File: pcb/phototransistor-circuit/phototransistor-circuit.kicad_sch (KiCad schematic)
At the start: 5 parts

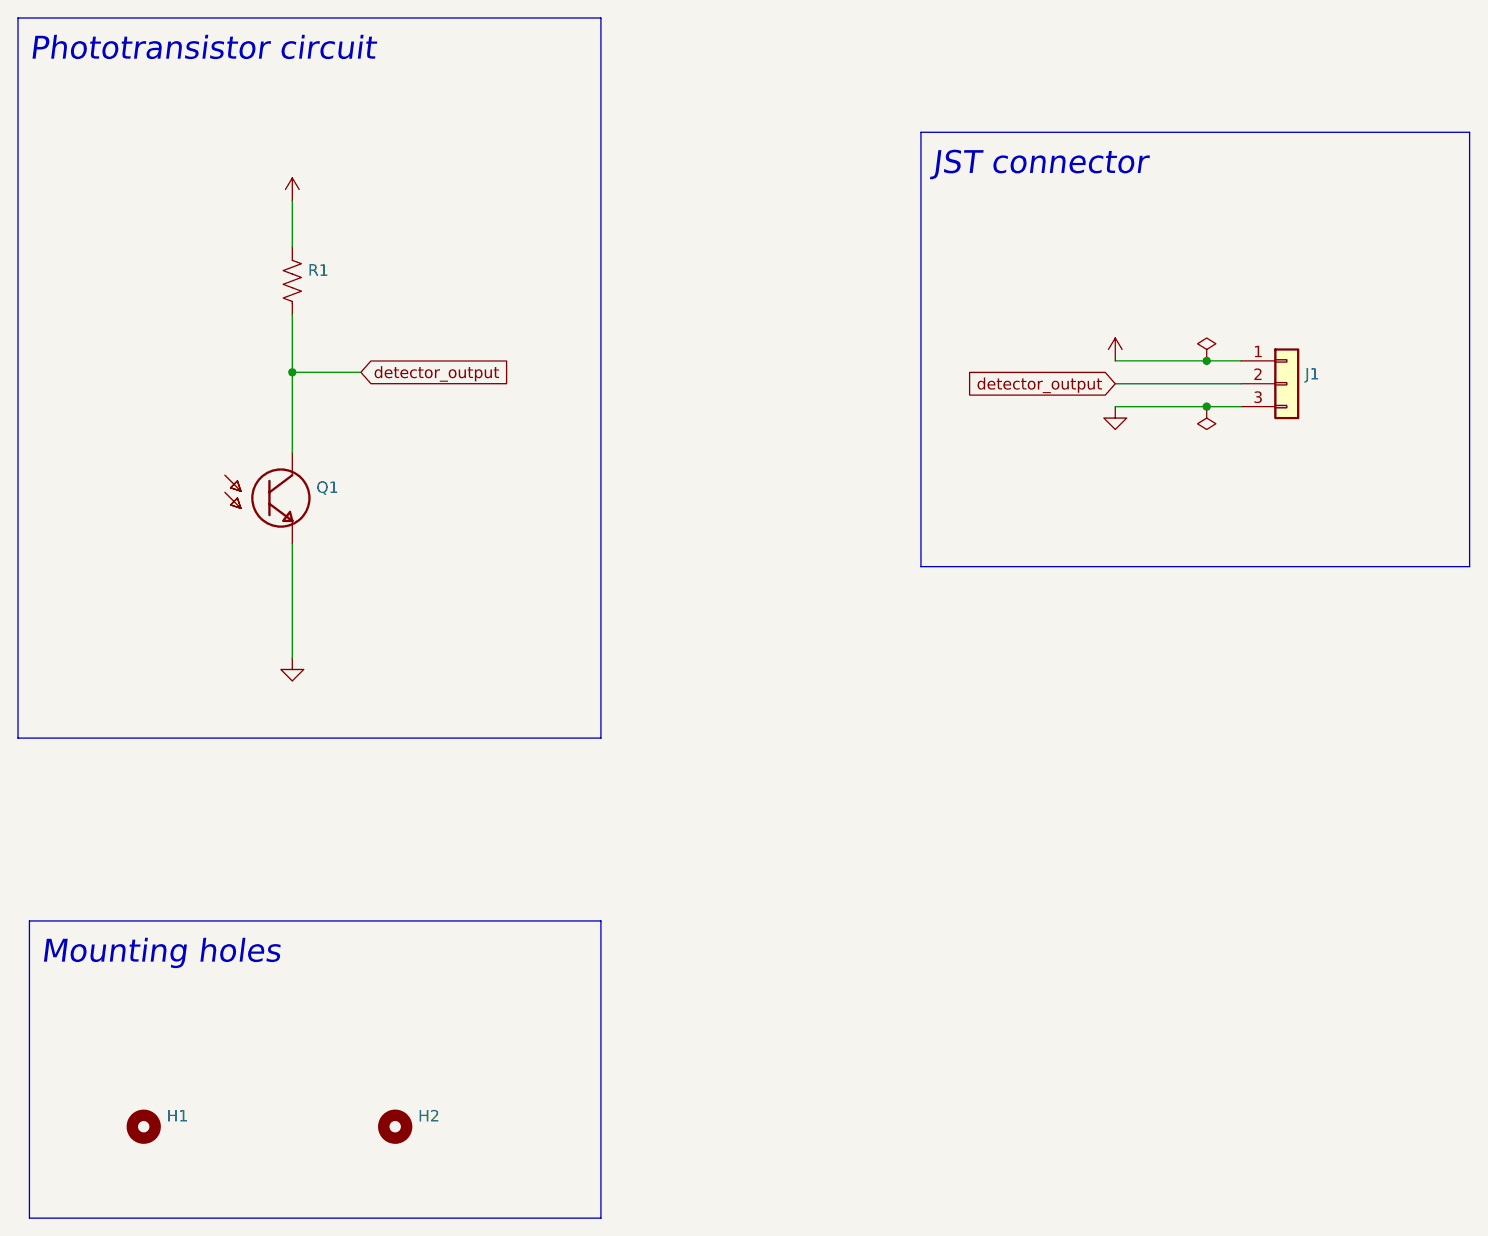
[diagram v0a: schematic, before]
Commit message: change vcc to 3v3
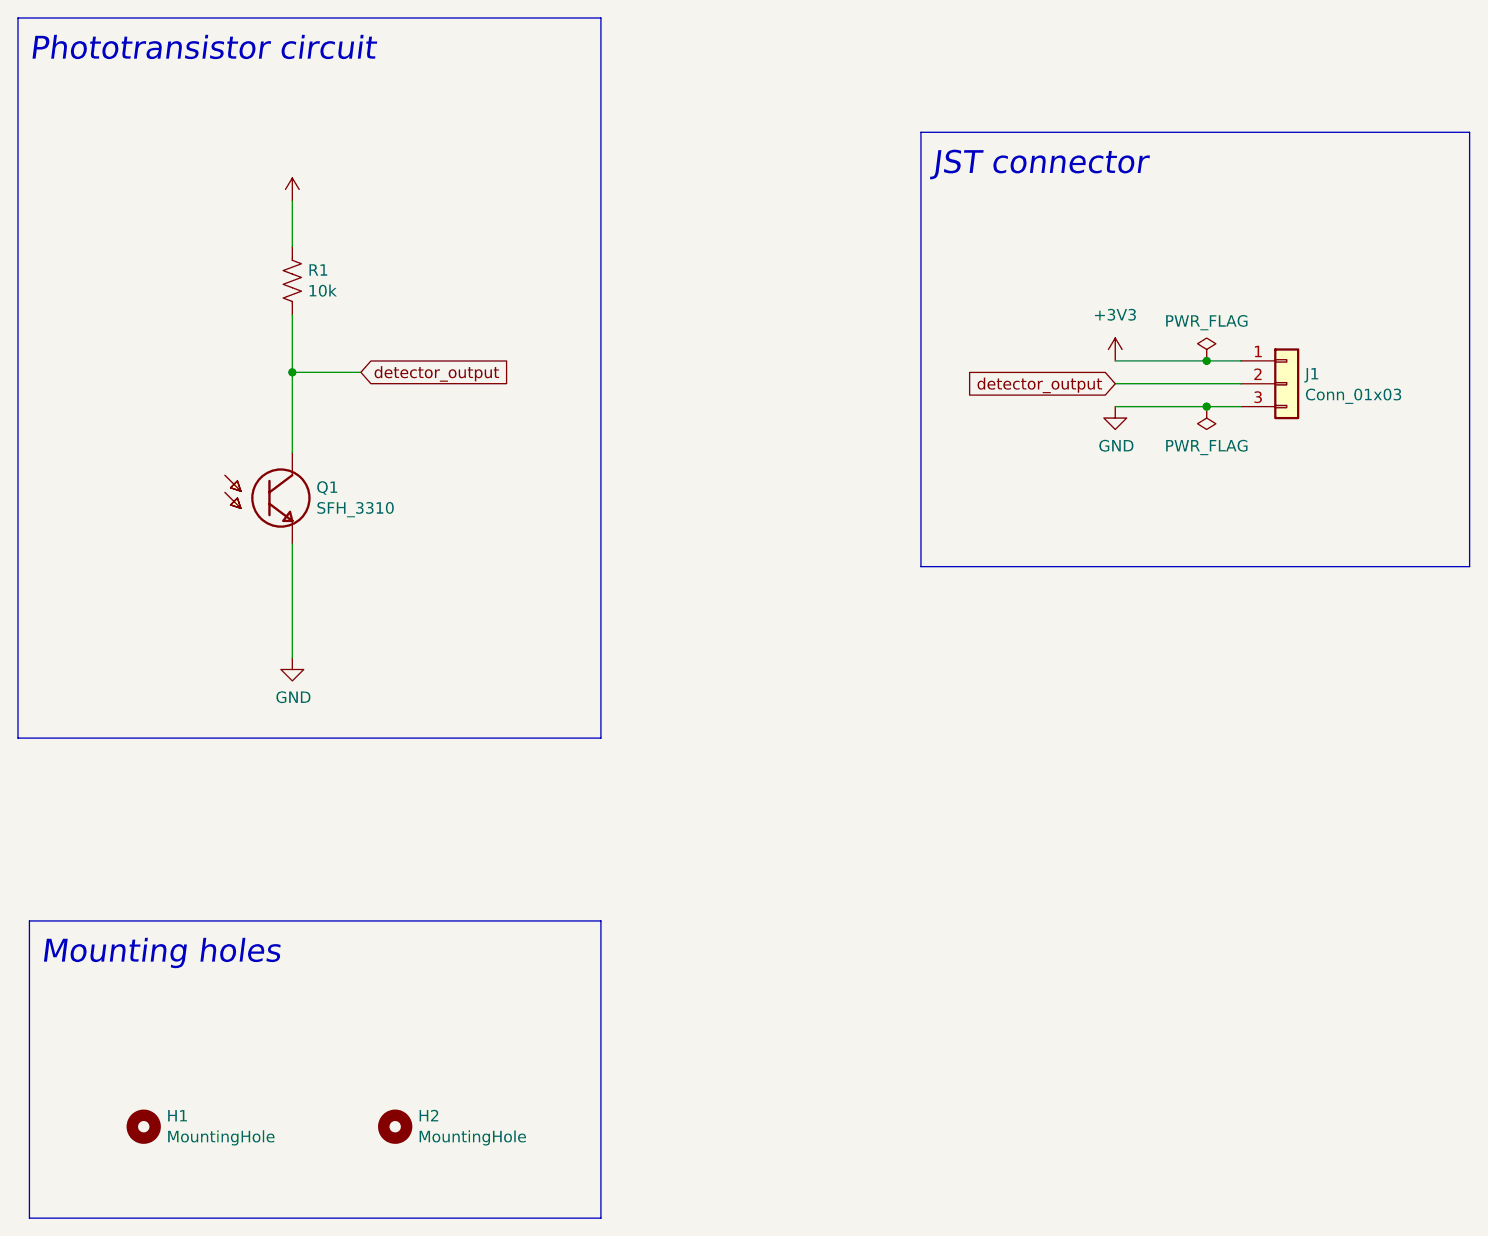
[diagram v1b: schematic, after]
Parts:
- H1, H2: value (none) -> MountingHole; footprint (none) -> MountingHole:MountingHole_3.2mm_M3
- J1: value (none) -> Conn_01x03; footprint (none) -> Connector_JST:JST_PH_B3B-PH-K_1x03_P2.00mm_Vertical
- Q1: value (none) -> SFH_3310; footprint (none) -> SFH_3310:XDCR_SFH_3310
- R1: value (none) -> 10k; footprint (none) -> Resistor_THT:R_Axial_DIN0207_L6.3mm_D2.5mm_P10.16mm_Horizontal
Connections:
- net VCC renamed +3V3
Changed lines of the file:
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@@
       (effects (font (size 1.27 1.27)) (justify left))
     )
-    (property "Value" "" (id 1) (at 64.897 96.393 0)
+    (property "Value" "SFH_3310" (id 1) (at 64.897 96.393 0)
       (effects (font (size 1.27 1.27)) (justify left))
     )
-    (property "Footprint" "" (id 2) (at 59.69 95.25 0)
+    (property "Footprint" "SFH_3310:XDCR_SFH_3310" (id 2) (at 59.69 95.25 0)
       (effects (font (size 1.27 1.27)) (justify left bottom) hide)
     )
@@
       (effects (font (size 1.27 1.27)) (justify left))
     )
-    (property "Value" "" (id 1) (at 63.9572 72.263 0)
+    (property "Value" "10k" (id 1) (at 63.9572 72.263 0)
       (effects (font (size 1.27 1.27)) (justify left))
     )
-    (property "Footprint" "" (id 2) (at 63.246 71.374 90)
+    (property "Footprint" "Resistor_THT:R_Axial_DIN0207_L6.3mm_D2.5mm_P10.16mm_Horizontal" (id 2) (at 63.246 71.374 90)
       (effects (font (size 1.27 1.27)) hide)
     )
@@
     (pin "2")
   )
-  (symbol (lib_id "power:VCC") (at 62.23 62.23 0) (unit 1)
-    (in_bom yes) (on_board yes)
-    (property "Reference" "#PWR01" (id 0) (at 62.23 66.04 0)
-      (effects (font (size 1.27 1.27)) hide)
-    )
-    (property "Value" "" (id 1) (at 62.6618 57.8358 0))
-    (property "Footprint" "" (id 2) (at 62.23 62.23 0)
-      (effects (font (size 1.27 1.27)) hide)
-    )
-    (property "Datasheet" "" (id 3) (at 62.23 62.23 0)
-      (effects (font (size 1.27 1.27)) hide)
-    )
-    (pin "1")
-  )
   (symbol (lib_id "power:GND") (at 62.23 113.03 0) (unit 1)
     (in_bom yes) (on_board yes)
@@
       (effects (font (size 1.27 1.27)) hide)
     )
-    (property "Value" "" (id 1) (at 62.357 117.4242 0))
+    (property "Value" "GND" (id 1) (at 62.357 117.4242 0))
     (property "Footprint" "" (id 2) (at 62.23 113.03 0)
       (effects (font (size 1.27 1.27)) hide)
@@
       (effects (font (size 1.27 1.27)) (justify left))
     )
-    (property "Value" "" (id 1) (at 48.26 166.243 0)
+    (property "Value" "MountingHole" (id 1) (at 48.26 166.243 0)
       (effects (font (size 1.27 1.27)) (justify left))
     )
-    (property "Footprint" "" (id 2) (at 45.72 165.1 0)
+    (property "Footprint" "MountingHole:MountingHole_3.2mm_M3" (id 2) (at 45.72 165.1 0)
       (effects (font (size 1.27 1.27)) hide)
     )
@@
       (effects (font (size 1.27 1.27)) (justify left))
     )
-    (property "Value" "" (id 1) (at 76.2 166.243 0)
+    (property "Value" "MountingHole" (id 1) (at 76.2 166.243 0)
       (effects (font (size 1.27 1.27)) (justify left))
     )
-    (property "Footprint" "" (id 2) (at 73.66 165.1 0)
+    (property "Footprint" "MountingHole:MountingHole_3.2mm_M3" (id 2) (at 73.66 165.1 0)
       (effects (font (size 1.27 1.27)) hide)
     )
@@
       (effects (font (size 1.27 1.27)) (justify left))
     )
-    (property "Value" "" (id 1) (at 174.752 83.7946 0)
+    (property "Value" "Conn_01x03" (id 1) (at 174.752 83.7946 0)
       (effects (font (size 1.27 1.27)) (justify left))
     )
-    (property "Footprint" "" (id 2) (at 172.72 82.55 0)
+    (property "Footprint" "Connector_JST:JST_PH_B3B-PH-K_1x03_P2.00mm_Vertical" (id 2) (at 172.72 82.55 0)
       (effects (font (size 1.27 1.27)) hide)
     )
@@
     (pin "3")
   )
-  (symbol (lib_id "power:VCC") (at 153.67 80.01 0) (unit 1)
-    (in_bom yes) (on_board yes)
-    (property "Reference" "#PWR03" (id 0) (at 153.67 83.82 0)
-      (effects (font (size 1.27 1.27)) hide)
-    )
-    (property "Value" "" (id 1) (at 154.1018 75.6158 0))
-    (property "Footprint" "" (id 2) (at 153.67 80.01 0)
-      (effects (font (size 1.27 1.27)) hide)
-    )
-    (property "Datasheet" "" (id 3) (at 153.67 80.01 0)
-      (effects (font (size 1.27 1.27)) hide)
-    )
-    (pin "1")
-  )
   (symbol (lib_id "power:GND") (at 153.67 85.09 0) (unit 1)
     (in_bom yes) (on_board yes)
@@
       (effects (font (size 1.27 1.27)) hide)
     )
-    (property "Value" "" (id 1) (at 153.797 89.4842 0))
+    (property "Value" "GND" (id 1) (at 153.797 89.4842 0))
     (property "Footprint" "" (id 2) (at 153.67 85.09 0)
       (effects (font (size 1.27 1.27)) hide)
@@
       (effects (font (size 1.27 1.27)) hide)
     )
-    (property "Value" "" (id 1) (at 163.83 75.6158 0))
+    (property "Value" "PWR_FLAG" (id 1) (at 163.83 75.6158 0))
     (property "Footprint" "" (id 2) (at 163.83 80.01 0)
       (effects (font (size 1.27 1.27)) hide)
@@
       (effects (font (size 1.27 1.27)) hide)
     )
-    (property "Value" "" (id 1) (at 163.83 89.4842 0))
+    (property "Value" "PWR_FLAG" (id 1) (at 163.83 89.4842 0))
     (property "Footprint" "" (id 2) (at 163.83 85.09 0)
       (effects (font (size 1.27 1.27)) hide)
     )
     (property "Datasheet" "~" (id 3) (at 163.83 85.09 0)
+      (effects (font (size 1.27 1.27)) hide)
+    )
+    (pin "1")
+  )
+  (symbol (lib_id "power:+3V3") (at 62.23 62.23 0) (unit 1)
+    (in_bom yes) (on_board yes) (fields_autoplaced)
+    (property "Reference" "#PWR?" (id 0) (at 62.23 66.04 0)
+      (effects (font (size 1.27 1.27)) hide)
+    )
+    (property "Value" "" (id 1) (at 62.23 57.15 0))
+    (property "Footprint" "" (id 2) (at 62.23 62.23 0)
+      (effects (font (size 1.27 1.27)) hide)
+    )
+    (property "Datasheet" "" (id 3) (at 62.23 62.23 0)
+      (effects (font (size 1.27 1.27)) hide)
+    )
+    (pin "1")
+  )
+  (symbol (lib_id "power:+3V3") (at 153.67 80.01 0) (unit 1)
+    (in_bom yes) (on_board yes) (fields_autoplaced)
+    (property "Reference" "#PWR?" (id 0) (at 153.67 83.82 0)
+      (effects (font (size 1.27 1.27)) hide)
+    )
+    (property "Value" "+3V3" (id 1) (at 153.67 74.93 0))
+    (property "Footprint" "" (id 2) (at 153.67 80.01 0)
+      (effects (font (size 1.27 1.27)) hide)
+    )
+    (property "Datasheet" "" (id 3) (at 153.67 80.01 0)
       (effects (font (size 1.27 1.27)) hide)
     )
@@
       (reference "#FLG0102") (unit 1) (value "PWR_FLAG") (footprint "")
     )
-    (path "/00000000-0000-0000-0000-0000626b70e3"
-      (reference "#PWR01") (unit 1) (value "VCC") (footprint "")
-    )
     (path "/00000000-0000-0000-0000-0000626b7ded"
       (reference "#PWR02") (unit 1) (value "GND") (footprint "")
-    )
-    (path "/00000000-0000-0000-0000-0000626c1c52"
-      (reference "#PWR03") (unit 1) (value "VCC") (footprint "")
     )
     (path "/00000000-0000-0000-0000-0000626c2331"
       (reference "#PWR04") (unit 1) (value "GND") (footprint "")
     )
+    (path "/70cda344-73be-4466-a097-1fd56f3b19e2"
+      (reference "#PWR?") (unit 1) (value "+3V3") (footprint "")
+    )
+    (path "/dffcf68d-1dc4-432b-936a-b761a573d792"
+      (reference "#PWR?") (unit 1) (value "+3V3") (footprint "")
+    )
     (path "/00000000-0000-0000-0000-0000626bf88c"

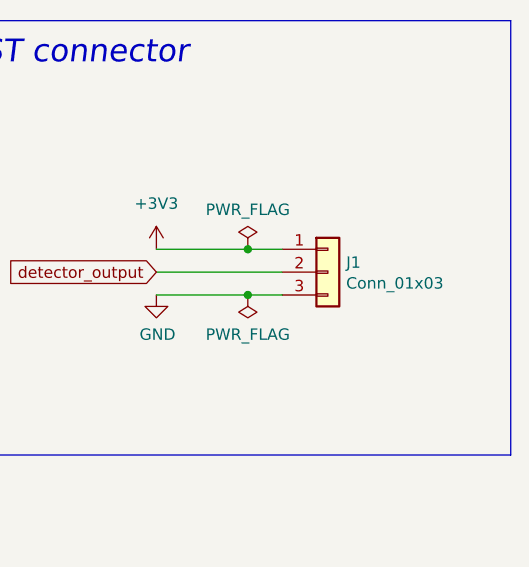
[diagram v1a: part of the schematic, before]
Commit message: update connector footprint to b3b-xh connector
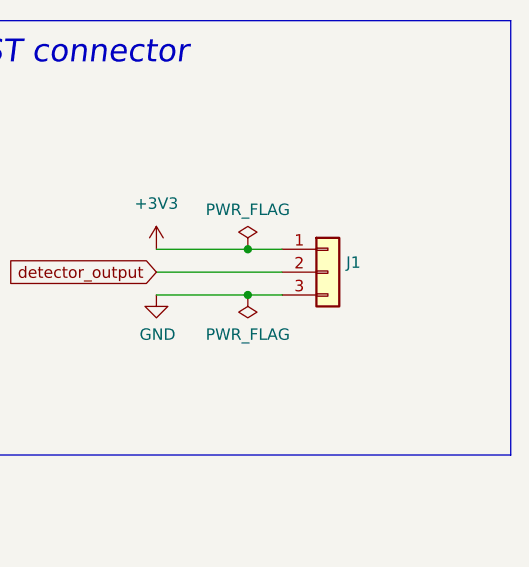
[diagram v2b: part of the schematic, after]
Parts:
- J1: value Conn_01x03 -> (none); footprint Connector_JST:JST_PH_B3B-PH-K_1x03_P2.00mm_Vertical -> (none)
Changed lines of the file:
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@@
       (effects (font (size 1.27 1.27)) (justify left))
     )
-    (property "Value" "Conn_01x03" (id 1) (at 174.752 83.7946 0)
+    (property "Value" "" (id 1) (at 174.752 83.7946 0)
       (effects (font (size 1.27 1.27)) (justify left))
     )
-    (property "Footprint" "Connector_JST:JST_PH_B3B-PH-K_1x03_P2.00mm_Vertical" (id 2) (at 172.72 82.55 0)
+    (property "Footprint" "" (id 2) (at 172.72 82.55 0)
       (effects (font (size 1.27 1.27)) hide)
     )
@@
   (symbol (lib_id "power:+3V3") (at 62.23 62.23 0) (unit 1)
     (in_bom yes) (on_board yes) (fields_autoplaced)
-    (property "Reference" "#PWR?" (id 0) (at 62.23 66.04 0)
+    (property "Reference" "#PWR0101" (id 0) (at 62.23 66.04 0)
       (effects (font (size 1.27 1.27)) hide)
     )
@@
   (symbol (lib_id "power:+3V3") (at 153.67 80.01 0) (unit 1)
     (in_bom yes) (on_board yes) (fields_autoplaced)
-    (property "Reference" "#PWR?" (id 0) (at 153.67 83.82 0)
+    (property "Reference" "#PWR0102" (id 0) (at 153.67 83.82 0)
       (effects (font (size 1.27 1.27)) hide)
     )
@@
     )
     (path "/70cda344-73be-4466-a097-1fd56f3b19e2"
-      (reference "#PWR?") (unit 1) (value "+3V3") (footprint "")
+      (reference "#PWR0101") (unit 1) (value "+3V3") (footprint "")
     )
     (path "/dffcf68d-1dc4-432b-936a-b761a573d792"
-      (reference "#PWR?") (unit 1) (value "+3V3") (footprint "")
+      (reference "#PWR0102") (unit 1) (value "+3V3") (footprint "")
     )
     (path "/00000000-0000-0000-0000-0000626bf88c"
@@
     )
     (path "/00000000-0000-0000-0000-0000626c1847"
-      (reference "J1") (unit 1) (value "Conn_01x03") (footprint "Connector_JST:JST_PH_B3B-PH-K_1x03_P2.00mm_Vertical")
+      (reference "J1") (unit 1) (value "Conn_01x03") (footprint "Connector_JST:JST_XH_B3B-XH-A_1x03_P2.50mm_Vertical")
     )
     (path "/00000000-0000-0000-0000-0000626b5645"
